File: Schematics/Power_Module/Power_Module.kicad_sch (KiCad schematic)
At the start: 0 parts

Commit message: hybrid power board, with preserved OG Power board  - still hybrid still needs review and silkscreen
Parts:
- added C1, C2, C3: 4.7uF, Capacitor_SMD:C_0805_2012Metric, symbol Device:C
- added C10, C4, C47, C48, C5, C6, C7, C9: 100nF, Capacitor_SMD:C_0603_1608Metric, symbol Device:C
- added C11, C13, C16, C17, C18, C8: 22uF, Capacitor_SMD:C_0805_2012Metric, symbol Device:C
- added C12, C14, C15: 100uF, Capacitor_SMD:CP_Elec_6.3x5.9, symbol Device:C_Polarized
- added C19, C20: 10uF, Capacitor_SMD:C_0603_1608Metric, symbol Device:C
- added C21, C22, C44, C45, C46: 0.1u, Capacitor_SMD:C_0603_1608Metric, symbol Device:C
- added C23, C24: 10p, Capacitor_SMD:C_0603_1608Metric, symbol Device:C
- added C25, C26, C27, C28, C29, C30, C31, C32: 100n, Capacitor_SMD:C_0402_1005Metric, symbol Device:C
- added C33, C36: 10n, Capacitor_SMD:C_0603_1608Metric, symbol Device:C
- added C34, C35, C37, C38: 1uF, Capacitor_SMD:C_0805_2012Metric, symbol Device:C_Polarized
- added C39, C40, C41, C42, C43: 1uF, Capacitor_SMD:C_0603_1608Metric, symbol Device:C
- added C49, C50: 0.1u, Capacitor_SMD:C_0603_1608Metric_Pad1.08x0.95mm_HandSolder, symbol Device:C
- added D1: 3.3V_A PWR (GRN), LED_SMD:LED_0805_2012Metric, symbol Device:LED
- added D2: 5.0V_A PWR (RED), LED_SMD:LED_0805_2012Metric, symbol Device:LED
- added D3: 3.3V_B PWR (GRN), LED_SMD:LED_0805_2012Metric, symbol Device:LED
- added D5, D8: DB_LED (YLW), LED_SMD:LED_0603_1608Metric, symbol Device:LED
- added FB1, FB2: 100R, Resistor_SMD:R_0805_2012Metric, symbol Device:FerriteBead
- added J1: ScrewSwitch B, footprints:CONN_2-1445057-2_TYCO, symbol CONN_2-1445057-2_TYCO:2-1445057-2
- added J2: ScrewSwitch A, footprints:CONN_2-1445057-2_TYCO, symbol CONN_2-1445057-2_TYCO:2-1445057-2
- added J3: Battery A, footprints:CONN_2-1445057-2_TYCO, symbol CONN_2-1445057-2_TYCO:2-1445057-2
- added J4: USB_C_Female_USB2_Small, footprints:USB_C_DB-108PWB, symbol USB_C:USB_C_Female_USB2_Small
- added J5: Battery B, footprints:CONN_2-1445057-2_TYCO, symbol CONN_2-1445057-2_TYCO:2-1445057-2
- added J6: Stack Male Edge Connector, Connector_PCBEdge:BUS_PCIexpress_x1, symbol EdgeConnector:Stack Male Edge Connector
- added J7, J8: SWD_B, SWD_Header:SWD_PinHeader_1x04_P2.54mm_Horizontal_SMD, symbol EdgeConnector:SWD_01x04_Pin
- added JP1: USB_V_EN, Jumper:SolderJumper-2_P1.3mm_Open_RoundedPad1.0x1.5mm, symbol Jumper:Jumper_2_Open
- added L1, L3: 5.6uH, Inductor_SMD:L_Bourns_SRN8040TA, symbol Device:L
- added L2: 6.8uH, Inductor_SMD:L_Bourns_SRN8040TA, symbol Device:L
- added Q1, Q2: AO4447A, Package_SO:SOIC-8_3.9x4.9mm_P1.27mm, symbol Transistor_FET:IRF7404
- added R1, R23, R25, R26, R28, R3: 100k, Resistor_SMD:R_0603_1608Metric, symbol Device:R
- added R10: 56k, Resistor_SMD:R_0603_1608Metric, symbol Device:R
- added R11: 7.5k, Resistor_SMD:R_0603_1608Metric, symbol Device:R
- added R12, R14, R15, R5: 30k, Resistor_SMD:R_0603_1608Metric, symbol Device:R
- added R13, R21, R22, R6: 10k, Resistor_SMD:R_0603_1608Metric, symbol Device:R
- added R16: 1.5k, Resistor_SMD:R_0603_1608Metric, symbol Device:R
- added R17, R18: 5.1k, Resistor_SMD:R_0603_1608Metric, symbol Device:R
- added R19, R20: 680R, Resistor_SMD:R_0603_1608Metric, symbol Device:R
- added R2, R4: 22k, Resistor_SMD:R_0603_1608Metric, symbol Device:R
- added R24: BT0_A, Resistor_SMD:R_0603_1608Metric_Pad0.98x0.95mm_HandSolder, symbol Device:R
- added R27: BT0_B, Resistor_SMD:R_0603_1608Metric_Pad0.98x0.95mm_HandSolder, symbol Device:R
- added R7, R9: 3.3k, Resistor_SMD:R_0603_1608Metric, symbol Device:R
- added R8: 2.4k, Resistor_SMD:R_0603_1608Metric, symbol Device:R
- added TP1: BT_A, TestPoint:TestPoint_Pad_2.0x2.0mm, symbol Connector:TestPoint
- added TP10: B.S, TestPoint:TestPoint_Pad_1.5x1.5mm, symbol Connector:TestPoint
- added TP11: 3B.C.S, TestPoint:TestPoint_Pad_1.5x1.5mm, symbol Connector:TestPoint
- added TP12: 3ACS, TestPoint:TestPoint_Pad_1.5x1.5mm, symbol Connector:TestPoint
- added TP13: 5ACS, TestPoint:TestPoint_Pad_1.5x1.5mm, symbol Connector:TestPoint
- added TP16: PA7B, TestPoint:TestPoint_Pad_1.5x1.5mm, symbol Connector:TestPoint
- added TP17: PA6B, TestPoint:TestPoint_Pad_1.5x1.5mm, symbol Connector:TestPoint
- added TP2: BT_B, TestPoint:TestPoint_Pad_2.0x2.0mm, symbol Connector:TestPoint
- added TP3: GND2, TestPoint:TestPoint_Pad_2.0x2.0mm, symbol Connector:TestPoint
- added TP4: GND1, TestPoint:TestPoint_Pad_2.0x2.0mm, symbol Connector:TestPoint
- added TP5: 3v3_A, TestPoint:TestPoint_Pad_2.0x2.0mm, symbol Connector:TestPoint
- added TP6: 5V_A, TestPoint:TestPoint_Pad_2.0x2.0mm, symbol Connector:TestPoint
- added TP7: 3v3_B, TestPoint:TestPoint_Pad_2.0x2.0mm, symbol Connector:TestPoint
- added TP8: 5VSENS, TestPoint:TestPoint_Pad_1.5x1.5mm, symbol Connector:TestPoint
- added TP9: A.S, TestPoint:TestPoint_Pad_1.5x1.5mm, symbol Connector:TestPoint
- added U1, U2, U3: LMR51430XDDCR, Package_TO_SOT_SMD:SOT-23-6_Handsoldering, symbol QRET_Buck_PSU-symbols:LMR51430XDDCR
- added U10: ISO1042BDWVR, ISO1042:SOIC-8 ISO1042BDWV, symbol ISO1042BQDWVQ1:ISO1042BQDWVQ1
- added U11, U12, U13, U14, U15: LM66100DCKR, LMR66100:SC-70-6_Handsoldering, symbol QRET_Buck_PSU-symbols:LM66100DCKR
- added U16: SCM3721ASA, Package_SO:SOIC-8_3.9x4.9mm_P1.27mm, symbol SCM3721ASA:SCM3721ASA
- added U4, U5: STM32F103C8T6, Package_QFP:LQFP-48_7x7mm_P0.5mm, symbol MCU_ST_STM32F1:STM32F103C8Tx
- added U6, U7, U8: ACS37041KLHBLT-010B3, footprints:APS12628LLHALTBAP_HandSolder, symbol ACS37041KLHBLT-010B3:ACS37041KLHBLT-010B3
- added U9: AMS1117-3.3, Package_TO_SOT_SMD:SOT-223-3_TabPin2, symbol Regulator_Linear:AMS1117-3.3
- added Y1: X322516MMB4SI, Crystal:Crystal_SMD_3225-4Pin_3.2x2.5mm, symbol Device:Crystal_GND24
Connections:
- new net: C7.1, L2.1, U2.2 (SW)
- new net: R10.2, R11.1, U2.4 (FB)
- new net: C7.2, U2.6 (CB)
- new net: C5.1, L1.1, U1.2 (SW)
- new net: C5.2, U1.6 (CB)
- new net: C19.1, J4.A4 (VBUS), J4.A9 (VBUS), J4.B4 (VBUS), J4.B9 (VBUS), U9.3 (VI)
- new net: TP17.1, U5.16 (PA6)
- new net: R3.2, R4.1, U1.4 (FB)
- new net: JP1.2 (B), U12.3 (*CE), U12.6 (VOUT)
- new net: D5.2 (A), R19.1
- new net: J2.2, Q1.5 (D), Q1.6 (D), Q1.7 (D), Q1.8 (D)
- new net: C9.1, L3.1, U3.2 (SW)
- new net: R1.2, R2.1, U3.4 (FB)
- new net: C9.2, U3.6 (CB)
- new net: D3.2 (A), R9.2
- new net: J1.1, J5.2
- new net: J4.A5 (CC1), R17.1
- new net: D1.2 (A), R7.2
- new net: D2.2 (A), R8.2
- new net: J2.1, J3.2
- new net: D8.2 (A), R20.1
- new net: TP16.1, U5.17 (PA7)
- new net: J4.B5 (CC2), R18.1
- new net: J1.2, Q2.5 (D), Q2.6 (D), Q2.7 (D), Q2.8 (D)
- new net 3.3VA_A: C33.1, C34.1, FB1.1, U4.9 (VDDA)
- new net 3.3VA_B: C36.1, C37.1, FB2.1, U5.9 (VDDA)
- new net 3.3V_A: C42.1, J6.A1 (3.3V_A), J6.A2 (3.3V_A), U14.1 (VIN), U6.2 (IP-)
- new net 3.3V_A_ACS_PWR: C44.1, U4.16 (PA6), U6.5 (VDD)
- new net 3.3V_A_CURR_SENSE: TP12.1, U4.14 (PA4), U6.4 (VOUT)
- new net 3.3V_A_Pre: C12.1, C16.1, C8.1, L1.2, R3.1, TP5.1, U6.1 (IP+)
- new net 3.3V_B: C39.1, J6.A7 (3.3V_B), J6.A8 (3.3V_B), U11.1 (VIN), U8.1 (IP+)
- new net 3.3V_B_ACS_PWR: C46.1, U5.18 (PB0), U8.5 (VDD)
- new net 3.3V_B_CURR_SENSE: TP11.1, U5.19 (PB1), U8.4 (VOUT)
- new net 3.3V_B_Pre: C13.1, C15.1, C18.1, L3.2, R1.1, TP7.1, U8.2 (IP-)
- new net 5.0V_A: C22.2, J6.A4 (5.0V_A), J6.A5 (5.0V_A), R14.1, R8.1, U10.8 (VCC2), U7.1 (IP+)
- new net 5.0V_A_ACS_PWR: C45.1, U4.12 (PA2), U7.5 (VDD)
- new net 5.0V_A_CURR_SENSE: TP13.1, U4.15 (PA5), U7.4 (VOUT)
- new net 5.0V_A_Pre: C11.1, C14.1, C17.1, L2.2, R10.1, TP6.1, U7.2 (IP-)
- new net 5.0V_A_SENSE: R14.2, R15.1, TP8.1, U4.11 (PA1)
- new net BATT_A: C1.1, C10.1, C2.1, C4.1, J6.B1 (BATT_A), J6.B2 (BATT_A), J6.B3 (BATT_A), Q1.1 (S), Q1.2 (S), Q1.3 (S), R5.1, TP1.1, U1.3 (VIN), U1.5 (EN), U2.3 (VIN), U2.5 (EN)
- new net BATT_A_SENSE: R5.2, R6.1, TP9.1, U4.10 (PA0)
- new net BATT_B: C3.1, C6.1, J6.B7 (BATT_B), J6.B8 (BATT_B), J6.B9 (BATT_B), Q2.1 (S), Q2.2 (S), Q2.3 (S), R12.1, TP2.1, U3.3 (VIN), U3.5 (EN)
- new net BATT_B_SENSE: R12.2, R13.1, TP10.1, U5.11 (PA1)
- new net BOOT0_A: R23.2, R24.2, U4.44 (BOOT0)
- new net BOOT0_B: R26.2, R27.2, U5.44 (BOOT0)
- new net BOOT1_A: R25.2, U4.20 (PB2)
- new net BOOT1_B: R28.2, U5.20 (PB2)
- new net CAN_+: J6.B14 (CAN_H), U10.7 (CANH)
- new net CAN_-: J6.B13 (CAN_L), U10.6 (CANL)
- new net CAN_RX: U10.3 (RXD), U4.45 (PB8)
- new net CAN_TX: U10.2 (TXD), U4.46 (PB9)
- new net DB_LED_A: R19.2, U4.17 (PA7)
- new net DB_LED_B: R20.2, U5.29 (PA8)
- new net GND: C1.2, C10.2, C11.2, C12.2, C14.2, C16.2, C17.2, C2.2, C21.1, C22.1, C26.1, C27.1, C28.1, C29.1, C33.2, C34.2, C35.2, C4.2, C42.2, C43.2, C44.2, C45.2, C48.2, C49.1, C8.2, D1.1 (K), D2.1 (K), D5.1 (K), J3.1, J6.A3 (GND_A), J6.A6 (GND_A), J6.B4 (GND_A), J6.B5 (GND_A), J6.B6 (GND_A), J8.1 (GND), Q1.4 (G), R11.2, R15.2, R23.1, R25.1, R4.2, R6.2, TP4.1, U1.1 (GND), U10.4 (GND1), U10.5 (GND2), U14.2 (GND), U14.5 (ST), U15.2 (GND), U15.5 (ST), U16.4 (GND1), U2.1 (GND), U4.23 (VSS), U4.35 (VSS), U4.47 (VSS), U4.8 (VSSA), U6.3 (GND), U7.3 (GND)
- new net GND2: C13.2, C15.2, C18.2, C19.2, C20.2, C23.2, C24.2, C25.1, C3.2, C30.1, C31.1, C32.1, C36.2, C37.2, C38.2, C39.2, C40.2, C41.2, C46.2, C47.2, C50.2, C6.2, D3.1 (K), D8.1 (K), J4.A1 (GND), J4.A12 (GND), J4.B1 (GND), J4.B12 (GND), J5.1, J6.A12 (GND_B), J6.A9 (GND_B), J6.B10 (GND_B), J6.B11 (GND_B), J6.B12 (GND_B), J7.1 (GND), Q2.4 (G), R13.2, R17.2, R18.2, R2.2, R26.1, R28.1, TP3.1, U11.2 (GND), U11.5 (ST), U12.2 (GND), U12.5 (ST), U13.2 (GND), U13.5 (ST), U16.5 (GND2), U3.1 (GND), U5.23 (VSS), U5.35 (VSS), U5.47 (VSS), U5.8 (VSSA), U8.3 (GND), U9.1 (GND), Y1.2, Y1.4
- new net OSC_IN: C23.1, U5.5 (PD0), Y1.1
- new net OSC_OUT: C24.1, U5.6 (PD1), Y1.3
- new net RX_A: U16.2 (Out_A), U4.31 (PA10)
- new net RX_B: U16.6 (Out_B), U5.31 (PA10)
- new net STM_RESET_A: C48.1, R22.1, U4.7 (NRST)
- new net STM_RESET_B: C47.1, R21.1, U5.7 (NRST)
- new net SWCLK_A: J8.4 (SWCLK), U4.37 (PA14)
- new net SWCLK_B: J7.4 (SWCLK), U5.37 (PA14)
- new net SWDIO_A: J8.3 (SWDIO), U4.34 (PA13)
- new net SWDIO_B: J7.3 (SWDIO), U5.34 (PA13)
- new net TX_A: U16.3 (In_B), U4.30 (PA9)
- new net TX_B: U16.7 (In_A), U5.30 (PA9)
- new net USB_D+: J4.A6 (D+), J4.B6 (D+), R16.2, U5.33 (PA12)
- new net USB_D-: J4.A7 (D-), J4.B7 (D-), U5.32 (PA11)
- new net V_MUX_A: C21.2, C26.2, C27.2, C28.2, C29.2, C35.1, C49.2, FB1.2, R22.2, R24.1, R7.1, U10.1 (VCC1), U14.3 (*CE), U14.6 (VOUT), U15.3 (*CE), U15.6 (VOUT), U16.1 (VDD1), U4.1 (VBAT), U4.24 (VDD), U4.36 (VDD), U4.48 (VDD)
- new net V_MUX_B: C25.2, C30.2, C31.2, C32.2, C38.1, C50.1, FB2.2, JP1.1 (A), R16.1, R21.2, R27.1, R9.1, U11.3 (*CE), U11.6 (VOUT), U13.3 (*CE), U13.6 (VOUT), U16.8 (VDD2), U5.1 (VBAT), U5.24 (VDD), U5.36 (VDD), U5.48 (VDD)
- new net V_REGUSB_B: C20.1, C40.1, U12.1 (VIN), U9.2 (VO)
- new net V_SWD_A: C43.1, J8.2 (3V3), U15.1 (VIN)
- new net V_SWD_B: C41.1, J7.2 (3V3), U13.1 (VIN)
- no-connect marks 0 -> 49
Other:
- removed sheet mcu
- removed sheet power
- note added: ""main""
- note added: ""passthru""
- note added: "A"
- note added: "ACS37041 draws ~12mA"
- note added: "B"
- note added: "B0 HIGH = PROGRAMMING MODE B0 LOW = RUN MEMORY"
- note added: "CONSIDER ADDING NTC TEMP SENSOR?"
- note added: "Edge Connector"
- note added: "FOLLOW LAYOUT EXAMPLE (9.4.2) FROM DATASHEET LMR51430: PFM @ 500kHz (simpler routing & higher efficiency)"
- note added: "Galvanic isolation barrier (we're not using isolation for primary modules)"
- note added: "Max Output: 2.5A"
- note added: "Mount connector at edge of board"
- note added: "Place 4mm from edge of board"
- note added: "Power Indicator LEDs"
- note added: "Primary 3.3V Buck Regulator"
- note added: "Primary 5.0V Buck Regulator"
- note added: "Primary Power Connectors (with RPP)"
- note added: "REDUCE COMPONENTS WHEREVER POSSIBLE -> CONSIDER REMOVING LM66100 & SOME AVDD FILTER CAPS"
- note added: "Rfbt=100k, Rfbb=22k Vout = ((Rfbt*0.6)/Rfbb)+0.6 Vout = 3.327V"
- note added: "Rfbt=56k, Rfbb=7.5k Vout = ((Rfbt*0.6)/Rfbb)+0.6 Vout = 5.080V"
- note added: "STM32 decoupling caps; place close to 3.3V pins"
- note added: "Secondary 3.3V Buck Regulator"
- note added: "Secondary Power Connectors (with RPP)"
- note added: "Vf=2.1V, I=1.8mA, R=680"
- note added: "Vin=3.3V, Vf=2.8V, R=0.15mA, R=3.3k"
- note added: "Vin=5.0V, Vf=2.0V, I=1.3mA, R=2.4k"
- note added: "[A/B] Digital Isolator"
- note added: "[A] Additional Filtering for Analogue VDD"
- note added: "[A] CANBUS Interface"
- note added: "[A] Debug LED"
- note added: "[A] Ideal Diodes (MUX)"
- note added: "[A] STM32 Boot Mode"
- note added: "[A] STM32 Decoupling Capacitors for VBAT/VDD"
- note added: "[A] Serial Wire Debug"
- note added: "[A] Voltage + Current Sensors"
- note added: "[B] Additional Filtering for Analogue VDD"
- note added: "[B] Crystal Oscillator"
- note added: "[B] Debug LED"
- note added: "[B] Ideal Diodes (MUX)"
- note added: "[B] STM32 Decoupling Capacitors for VBAT/VDD"
- note added: "[B] STM32 Reset"
- note added: "[B] Serial Wire Debug"
- note added: "[B] USB Connection"
- note added: "[B] Voltage + Current Sensors"

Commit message: init commit of power board hybrid revision
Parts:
- removed C13, C18: 22uF, Capacitor_SMD:C_0805_2012Metric, symbol Device:C
- removed C15: 100uF, Capacitor_SMD:CP_Elec_6.3x5.9, symbol Device:C_Polarized
- removed C23, C24: 10p, Capacitor_SMD:C_0603_1608Metric, symbol Device:C
- removed C25, C30, C31, C32: 100n, Capacitor_SMD:C_0402_1005Metric, symbol Device:C
- removed C3: 4.7uF, Capacitor_SMD:C_0805_2012Metric, symbol Device:C
- removed C36: 10n, Capacitor_SMD:C_0603_1608Metric, symbol Device:C
- removed C37, C38: 1uF, Capacitor_SMD:C_0805_2012Metric, symbol Device:C_Polarized
- removed C39, C41: 1uF, Capacitor_SMD:C_0603_1608Metric, symbol Device:C
- removed C46: 0.1u, Capacitor_SMD:C_0603_1608Metric, symbol Device:C
- removed C47, C6, C9: 100nF, Capacitor_SMD:C_0603_1608Metric, symbol Device:C
- removed C49, C50: 0.1u, Capacitor_SMD:C_0603_1608Metric_Pad1.08x0.95mm_HandSolder, symbol Device:C
- removed D3: 3.3V_B PWR (GRN), LED_SMD:LED_0805_2012Metric, symbol Device:LED
- removed D8: DB_LED (YLW), LED_SMD:LED_0603_1608Metric, symbol Device:LED
- removed FB2: 100R, Resistor_SMD:R_0805_2012Metric, symbol Device:FerriteBead
- removed J1: ScrewSwitch B, footprints:CONN_2-1445057-2_TYCO, symbol CONN_2-1445057-2_TYCO:2-1445057-2
- removed J5: Battery B, footprints:CONN_2-1445057-2_TYCO, symbol CONN_2-1445057-2_TYCO:2-1445057-2
- removed J7: SWD_B, SWD_Header:SWD_PinHeader_1x04_P2.54mm_Horizontal_SMD, symbol EdgeConnector:SWD_01x04_Pin
- removed JP1: USB_V_EN, Jumper:SolderJumper-2_P1.3mm_Open_RoundedPad1.0x1.5mm, symbol Jumper:Jumper_2_Open
- removed L3: 5.6uH, Inductor_SMD:L_Bourns_SRN8040TA, symbol Device:L
- removed Q2: AO4447A, Package_SO:SOIC-8_3.9x4.9mm_P1.27mm, symbol Transistor_FET:IRF7404
- removed R1, R26, R28: 100k, Resistor_SMD:R_0603_1608Metric, symbol Device:R
- removed R12: 30k, Resistor_SMD:R_0603_1608Metric, symbol Device:R
- removed R13, R21: 10k, Resistor_SMD:R_0603_1608Metric, symbol Device:R
- removed R2: 22k, Resistor_SMD:R_0603_1608Metric, symbol Device:R
- removed R20: 680R, Resistor_SMD:R_0603_1608Metric, symbol Device:R
- removed R27: BT0_B, Resistor_SMD:R_0603_1608Metric_Pad0.98x0.95mm_HandSolder, symbol Device:R
- removed R9: 3.3k, Resistor_SMD:R_0603_1608Metric, symbol Device:R
- removed TP10: B.S, TestPoint:TestPoint_Pad_1.5x1.5mm, symbol Connector:TestPoint
- removed TP11: 3B.C.S, TestPoint:TestPoint_Pad_1.5x1.5mm, symbol Connector:TestPoint
- removed TP16: PA7B, TestPoint:TestPoint_Pad_1.5x1.5mm, symbol Connector:TestPoint
- removed TP17: PA6B, TestPoint:TestPoint_Pad_1.5x1.5mm, symbol Connector:TestPoint
- removed TP2: BT_B, TestPoint:TestPoint_Pad_2.0x2.0mm, symbol Connector:TestPoint
- removed TP3: GND2, TestPoint:TestPoint_Pad_2.0x2.0mm, symbol Connector:TestPoint
- removed TP7: 3v3_B, TestPoint:TestPoint_Pad_2.0x2.0mm, symbol Connector:TestPoint
- removed U11, U13: LM66100DCKR, LMR66100:SC-70-6_Handsoldering, symbol QRET_Buck_PSU-symbols:LM66100DCKR
- removed U16: SCM3721ASA, Package_SO:SOIC-8_3.9x4.9mm_P1.27mm, symbol SCM3721ASA:SCM3721ASA
- removed U3: LMR51430XDDCR, Package_TO_SOT_SMD:SOT-23-6_Handsoldering, symbol QRET_Buck_PSU-symbols:LMR51430XDDCR
- removed U5: STM32F103C8T6, Package_QFP:LQFP-48_7x7mm_P0.5mm, symbol MCU_ST_STM32F1:STM32F103C8Tx
- removed U8: ACS37041KLHBLT-010B3, footprints:APS12628LLHALTBAP_HandSolder, symbol ACS37041KLHBLT-010B3:ACS37041KLHBLT-010B3
- removed Y1: X322516MMB4SI, Crystal:Crystal_SMD_3225-4Pin_3.2x2.5mm, symbol Device:Crystal_GND24
- R16: value 1.5k -> 5.1k; JLCPCB C22843 -> C23186
- R18: value 5.1k -> 1.5k; JLCPCB C23186 -> C22843
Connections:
- net V_MUX_B is gone; now on an unnamed net: R16.1
- net GND: now also C19.2, C20.2, U9.1 (GND)
- net GND2: now also R16.2; no longer C19.2, C20.2, J6.A12 (GND_B), J6.A9 (GND_B), J6.B10 (GND_B), J6.B11 (GND_B), J6.B12 (GND_B), R18.2, U9.1 (GND)
- net USB_D+: now also R18.2; no longer R16.2
- net V_MUX_A: no longer C21.2, U10.1 (VCC1), U14.3 (*CE), U14.6 (VOUT), U15.3 (*CE), U15.6 (VOUT)
- net 3.3V_MUX_A: now reaches U12.3 (*CE), U12.6 (VOUT)
- net 3.3V_MUX_A: now also C21.2, R18.1, U10.1 (VCC1), U14.3 (*CE), U14.6 (VOUT), U15.3 (*CE), U15.6 (VOUT)
- net at J4.A5 (CC1): no longer R17.1
- net at J4.B5 (CC2): now also R17.1; no longer R18.1
- net 3.3V_B: no longer names the net of J6.A7 (3.3V_B), J6.A8 (3.3V_B)
- net BATT_B: no longer names the net of J6.B7 (BATT_B), J6.B8 (BATT_B), J6.B9 (BATT_B)
- net V_REGUSB_B renamed 3.3V_REGUSB_A
- net 3.3V_REGUSB_A: no longer C20.1, U9.2 (VO)
- net V_SWD_A renamed 3.3V_SWD_A
- new net: J6.A12 (GND_B), J6.A9 (GND_B), J6.B10 (GND_B), J6.B11 (GND_B), J6.B12 (GND_B)
- new net V_REGUSB_A: C20.1, U9.2 (VO)
- no-connect marks 49 -> 30
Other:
- note added: "Additional Filtering for Analogue VDD"
- note added: "Can we support 3.3V current with just 2x1.1A pins?"
- note added: "Input is muxed between 24V and BAT_A"
- note added: "Maybe we need to change the RC time constant!!! Larger is better"
- note added: "STM32 Boot Mode"
- note added: "STM32 Decoupling Capacitors for VBAT/VDD"
- note added: "STM32 Reset"
- note added: "USB Connection"
- note removed: ""passthru""
- note removed: "B"
- note removed: "REDUCE COMPONENTS WHEREVER POSSIBLE -> CONSIDER REMOVING LM66100 & SOME AVDD FILTER CAPS"
- note removed: "Secondary 3.3V Buck Regulator"
- note removed: "Secondary Power Connectors (with RPP)"
- note removed: "[A/B] Digital Isolator"
- note removed: "[A] Additional Filtering for Analogue VDD"
- note removed: "[A] STM32 Boot Mode"
- note removed: "[A] STM32 Decoupling Capacitors for VBAT/VDD"
- note removed: "[B] Additional Filtering for Analogue VDD"
- note removed: "[B] Crystal Oscillator"
- note removed: "[B] Debug LED"
- note removed: "[B] Ideal Diodes (MUX)"
- note removed: "[B] STM32 Decoupling Capacitors for VBAT/VDD"
- note removed: "[B] STM32 Reset"
- note removed: "[B] Serial Wire Debug"
- note removed: "[B] USB Connection"
- note removed: "[B] Voltage + Current Sensors"
- moved on the sheet: C42, C43, U14, U15

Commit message: init commit of power design, with Bucks completed  - started Boost design
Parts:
- removed C1, C2: 4.7uF, Capacitor_SMD:C_0805_2012Metric, symbol Device:C
- removed C10, C4, C48, C5, C7: 100nF, Capacitor_SMD:C_0603_1608Metric, symbol Device:C
- removed C11, C16, C17, C8: 22uF, Capacitor_SMD:C_0805_2012Metric, symbol Device:C
- removed C12, C14: 100uF, Capacitor_SMD:CP_Elec_6.3x5.9, symbol Device:C_Polarized
- removed C19, C20: 10uF, Capacitor_SMD:C_0603_1608Metric, symbol Device:C
- removed C21, C22, C44, C45: 0.1u, Capacitor_SMD:C_0603_1608Metric, symbol Device:C
- removed C26, C27, C28, C29: 100n, Capacitor_SMD:C_0402_1005Metric, symbol Device:C
- removed C33: 10n, Capacitor_SMD:C_0603_1608Metric, symbol Device:C
- removed C34, C35: 1uF, Capacitor_SMD:C_0805_2012Metric, symbol Device:C_Polarized
- removed C40, C42, C43: 1uF, Capacitor_SMD:C_0603_1608Metric, symbol Device:C
- removed D1: 3.3V_A PWR (GRN), LED_SMD:LED_0805_2012Metric, symbol Device:LED
- removed D2: 5.0V_A PWR (RED), LED_SMD:LED_0805_2012Metric, symbol Device:LED
- removed D5: DB_LED (YLW), LED_SMD:LED_0603_1608Metric, symbol Device:LED
- removed FB1: 100R, Resistor_SMD:R_0805_2012Metric, symbol Device:FerriteBead
- removed J2: ScrewSwitch A, footprints:CONN_2-1445057-2_TYCO, symbol CONN_2-1445057-2_TYCO:2-1445057-2
- removed J3: Battery A, footprints:CONN_2-1445057-2_TYCO, symbol CONN_2-1445057-2_TYCO:2-1445057-2
- removed J4: USB_C_Female_USB2_Small, footprints:USB_C_DB-108PWB, symbol USB_C:USB_C_Female_USB2_Small
- removed J6: Stack Male Edge Connector, Connector_PCBEdge:BUS_PCIexpress_x1, symbol EdgeConnector:Stack Male Edge Connector
- removed J8: SWD_B, SWD_Header:SWD_PinHeader_1x04_P2.54mm_Horizontal_SMD, symbol EdgeConnector:SWD_01x04_Pin
- removed L1: 5.6uH, Inductor_SMD:L_Bourns_SRN8040TA, symbol Device:L
- removed L2: 6.8uH, Inductor_SMD:L_Bourns_SRN8040TA, symbol Device:L
- removed Q1: AO4447A, Package_SO:SOIC-8_3.9x4.9mm_P1.27mm, symbol Transistor_FET:IRF7404
- removed R10: 56k, Resistor_SMD:R_0603_1608Metric, symbol Device:R
- removed R11: 7.5k, Resistor_SMD:R_0603_1608Metric, symbol Device:R
- removed R14, R15, R5: 30k, Resistor_SMD:R_0603_1608Metric, symbol Device:R
- removed R16, R17: 5.1k, Resistor_SMD:R_0603_1608Metric, symbol Device:R
- removed R18: 1.5k, Resistor_SMD:R_0603_1608Metric, symbol Device:R
- removed R19: 680R, Resistor_SMD:R_0603_1608Metric, symbol Device:R
- removed R22, R6: 10k, Resistor_SMD:R_0603_1608Metric, symbol Device:R
- removed R23, R25, R3: 100k, Resistor_SMD:R_0603_1608Metric, symbol Device:R
- removed R24: BT0_A, Resistor_SMD:R_0603_1608Metric_Pad0.98x0.95mm_HandSolder, symbol Device:R
- removed R4: 22k, Resistor_SMD:R_0603_1608Metric, symbol Device:R
- removed R7: 3.3k, Resistor_SMD:R_0603_1608Metric, symbol Device:R
- removed R8: 2.4k, Resistor_SMD:R_0603_1608Metric, symbol Device:R
- removed TP1: BT_A, TestPoint:TestPoint_Pad_2.0x2.0mm, symbol Connector:TestPoint
- removed TP12: 3ACS, TestPoint:TestPoint_Pad_1.5x1.5mm, symbol Connector:TestPoint
- removed TP13: 5ACS, TestPoint:TestPoint_Pad_1.5x1.5mm, symbol Connector:TestPoint
- removed TP4: GND1, TestPoint:TestPoint_Pad_2.0x2.0mm, symbol Connector:TestPoint
- removed TP5: 3v3_A, TestPoint:TestPoint_Pad_2.0x2.0mm, symbol Connector:TestPoint
- removed TP6: 5V_A, TestPoint:TestPoint_Pad_2.0x2.0mm, symbol Connector:TestPoint
- removed TP8: 5VSENS, TestPoint:TestPoint_Pad_1.5x1.5mm, symbol Connector:TestPoint
- removed TP9: A.S, TestPoint:TestPoint_Pad_1.5x1.5mm, symbol Connector:TestPoint
- removed U1, U2: LMR51430XDDCR, Package_TO_SOT_SMD:SOT-23-6_Handsoldering, symbol QRET_Buck_PSU-symbols:LMR51430XDDCR
- removed U10: ISO1042BDWVR, ISO1042:SOIC-8 ISO1042BDWV, symbol ISO1042BQDWVQ1:ISO1042BQDWVQ1
- removed U12, U14, U15: LM66100DCKR, LMR66100:SC-70-6_Handsoldering, symbol QRET_Buck_PSU-symbols:LM66100DCKR
- removed U4: STM32F103C8T6, Package_QFP:LQFP-48_7x7mm_P0.5mm, symbol MCU_ST_STM32F1:STM32F103C8Tx
- removed U6, U7: ACS37041KLHBLT-010B3, footprints:APS12628LLHALTBAP_HandSolder, symbol ACS37041KLHBLT-010B3:ACS37041KLHBLT-010B3
- removed U9: AMS1117-3.3, Package_TO_SOT_SMD:SOT-223-3_TabPin2, symbol Regulator_Linear:AMS1117-3.3
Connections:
- no-connect marks 30 -> 0
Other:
- added sheet charger (battery_charger.kicad_sch)
- added sheet mcu (mcu.kicad_sch)
- added sheet power (power.kicad_sch)
- note removed: ""main""
- note removed: "A"
- note removed: "ACS37041 draws ~12mA"
- note removed: "Additional Filtering for Analogue VDD"
- note removed: "B0 HIGH = PROGRAMMING MODE B0 LOW = RUN MEMORY"
- note removed: "CONSIDER ADDING NTC TEMP SENSOR?"
- note removed: "Can we support 3.3V current with just 2x1.1A pins?"
- note removed: "Edge Connector"
- note removed: "FOLLOW LAYOUT EXAMPLE (9.4.2) FROM DATASHEET LMR51430: PFM @ 500kHz (simpler routing & higher efficiency)"
- note removed: "Galvanic isolation barrier (we're not using isolation for primary modules)"
- note removed: "Max Output: 2.5A"
- note removed: "Maybe we need to change the RC time constant!!! Larger is better"
- note removed: "Mount connector at edge of board"
- note removed: "Place 4mm from edge of board"
- note removed: "Power Indicator LEDs"
- note removed: "Primary 3.3V Buck Regulator"
- note removed: "Primary 5.0V Buck Regulator"
- note removed: "Primary Power Connectors (with RPP)"
- note removed: "Rfbt=100k, Rfbb=22k Vout = ((Rfbt*0.6)/Rfbb)+0.6 Vout = 3.327V"
- note removed: "Rfbt=56k, Rfbb=7.5k Vout = ((Rfbt*0.6)/Rfbb)+0.6 Vout = 5.080V"
- note removed: "STM32 Boot Mode"
- note removed: "STM32 Decoupling Capacitors for VBAT/VDD"
- note removed: "STM32 Reset"
- note removed: "STM32 decoupling caps; place close to 3.3V pins"
- note removed: "USB Connection"
- note removed: "Vf=2.1V, I=1.8mA, R=680"
- note removed: "Vin=3.3V, Vf=2.8V, R=0.15mA, R=3.3k"
- note removed: "Vin=5.0V, Vf=2.0V, I=1.3mA, R=2.4k"
- note removed: "[A] CANBUS Interface"
- note removed: "[A] Debug LED"
- note removed: "[A] Ideal Diodes (MUX)"
- note removed: "[A] Serial Wire Debug"
- note removed: "[A] Voltage + Current Sensors"

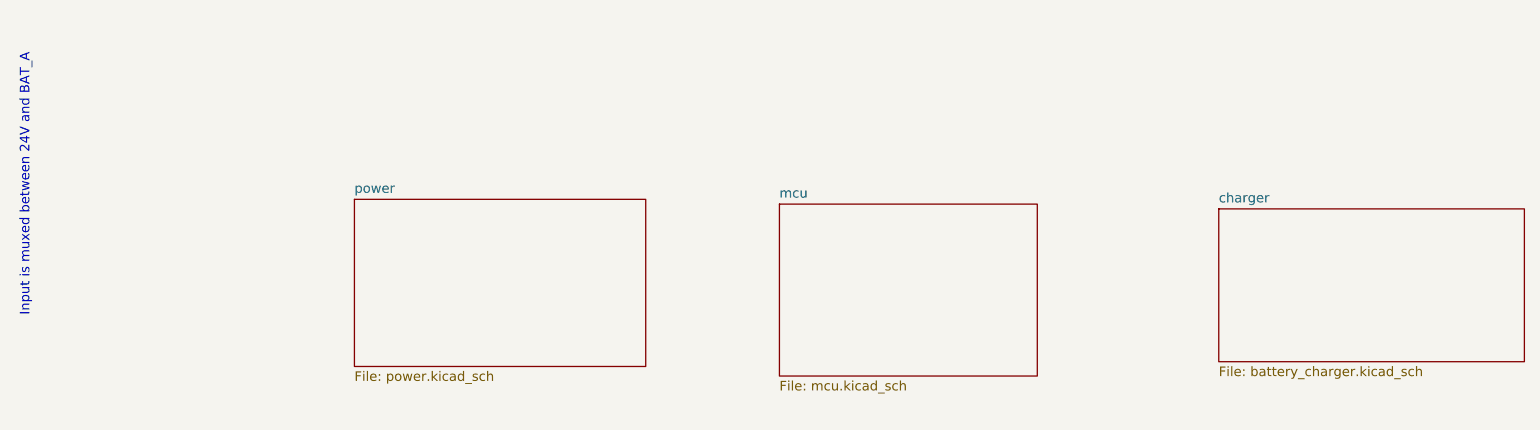
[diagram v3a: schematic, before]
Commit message: adding power ORing circuit
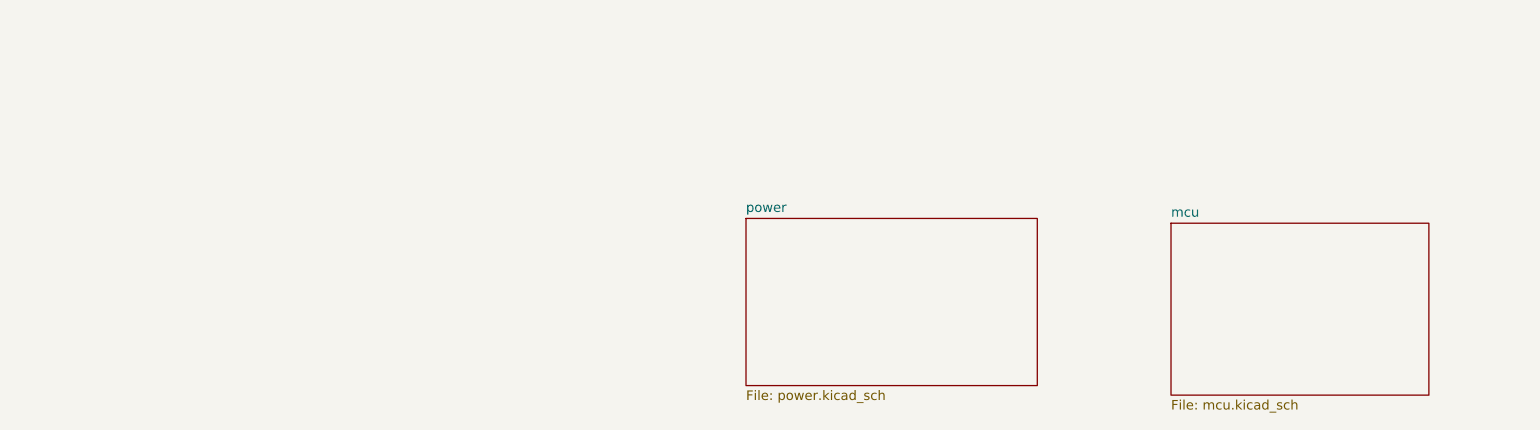
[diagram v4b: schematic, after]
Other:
- removed sheet charger
- note removed: "Input is muxed between 24V and BAT_A"
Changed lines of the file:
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@@
 		(comment 4 "GRID = 0.635mm")
 	)
-	(text "Input is muxed between 24V and BAT_A"
-		(exclude_from_sim no)
-		(at 6.35 76.2 90)
-		(effects
-			(font
-				(size 1.27 1.27)
-			)
-		)
-	)
 	(sheet
-		(at 106.68 78.74)
+		(at 158.75 81.28)
 		(size 34.29 22.86)
 		(fields_autoplaced yes)
@@
 		)
 		(property "Sheetname" "mcu"
-			(at 106.68 78.0284 0)
+			(at 158.75 80.5684 0)
 			(effects
 				(font
@@
 		)
 		(property "Sheetfile" "mcu.kicad_sch"
-			(at 106.68 102.1846 0)
+			(at 158.75 104.7246 0)
 			(effects
 				(font
@@
 	)
 	(sheet
-		(at 165.1 79.375)
-		(size 40.64 20.32)
-		(fields_autoplaced yes)
-		(stroke
-			(width 0.1524)
-			(type solid)
-		)
-		(fill
-			(color 0 0 0 0.0000)
-		)
-		(property "Sheetname" "charger"
-			(at 165.1 78.6634 0)
-			(effects
-				(font
-					(size 1.27 1.27)
-				)
-				(justify left bottom)
-			)
-		)
-		(property "Sheetfile" "battery_charger.kicad_sch"
-			(at 165.1 100.2796 0)
-			(effects
-				(font
-					(size 1.27 1.27)
-				)
-				(justify left top)
-			)
-		)
-		(instances
-			(project "Power_Module"
-				(path "/11b1f19b-ce82-4fce-baf6-0357ef2e3f24"
-					(page "4")
-				)
-			)
-		)
-	)
-	(sheet
-		(at 50.165 78.105)
+		(at 102.235 80.645)
 		(size 38.735 22.225)
 		(fields_autoplaced yes)
@@
 		)
 		(property "Sheetname" "power"
-			(at 50.165 77.3934 0)
+			(at 102.235 79.9334 0)
 			(effects
 				(font
@@
 		)
 		(property "Sheetfile" "power.kicad_sch"
-			(at 50.165 100.9146 0)
+			(at 102.235 103.4546 0)
 			(effects
 				(font

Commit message: current progress on power board
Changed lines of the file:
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@@
 		(comment 4 "GRID = 0.635mm")
+	)
+	(text_box "TODO\n - Add GSE_SENSE and 24V_CURR_SENSE\n - Review COMP C and R\n - Review 24V current sensing"
+		(exclude_from_sim no)
+		(at 113.03 115.0112 0)
+		(size 84.5312 15.0876)
+		(stroke
+			(width 0)
+			(type default)
+		)
+		(fill
+			(type none)
+		)
+		(effects
+			(font
+				(size 1.27 1.27)
+			)
+			(justify left top)
+		)
 	)
 	(sheet
